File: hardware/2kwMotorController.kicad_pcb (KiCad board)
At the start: 4 copper layers, 180 x 88 mm, 259 parts, among them M1 MOUNTING_HOLE, M2 MOUNTING_HOLE, M3 MOUNTING_HOLE, M4 MOUNTING_HOLE, M5 MOUNTING_HOLE, M6 MOUNTING_HOLE, P1 CONN_01X02_CBAT, P10 CONN_01_BRK, P11 CONN_01_M+, P12 CONN_01_M-, P13 CONN_01X02_MTMP, P14 CONN_01X02_BTMP, P2 CONN_01X02_FAN, P3 CONN_01X09, P4 CONN_02X05_JTAG, P5 CONN_01X03_UART, P6 CONN_01X03_CAN, P7 CONN_01X05_ENCODER, P8 CONN_01_V+, P9 CONN_01_V-, Q1 DMG4712SSS, Q10 PSMN021-100, Q2 DMG4712SSS, Q3 IRFP4468, Q4 PSMN021-100, Q5 IRFP4468, Q6 IRFP4468, Q7 IRFP4468, Q8 IRFP4468, Q9 IRFP4468, SW2 SW_PUSH, U1 LM358A, U10 MCP1501T-30E, U11 PDM1-S, U12 MIC5225-5.0, U13 TM4C1294KCPDT, U14 74LVCH2T45, U15 SN65HVD231D, U16 Si8045AA, U17 MIC4127, U18 MIC4127, U19 UCC27211, U2 LAH-100P, U20 Si8045AA, U21 74LVC1G17, U3 LOC110, U4 MCP6001, U5 ADA4805-1, U6 UCC27211, U7 MIC5225-5.0, U8 LT3471, U9 R-78E3.3-0.5, Y1 NX5032GA

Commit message: All DRC/ERC passed
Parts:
- removed the REF**1111 at (193.2, 109.0)
- removed the REF**1112 at (193.2, 109.5)
- removed the REF**1113 at (193.2, 110.0)
- removed the REF**121 at (153.0, 96.8)
- removed REF**122, REF**132, REF**142: VIA-0.6mm, 2kwMotorController:VIA-0.6mm
- removed the REF**131 at (153.5, 96.8)
- removed the REF**141 at (154.0, 96.8)
- added REF**: VIA-0.6mm, 2kwMotorController:VIA-0.6mm, F.Cu at (136.5, 48.5)
- added REF**: VIA-0.6mm, 2kwMotorController:VIA-0.6mm, F.Cu at (136.0, 48.5)
- added REF**: VIA-0.6mm, 2kwMotorController:VIA-0.6mm, F.Cu at (136.5, 47.0)
- added REF**: VIA-0.6mm, 2kwMotorController:VIA-0.6mm, F.Cu at (80.2, 30.0)
- added REF**: VIA-0.6mm, 2kwMotorController:VIA-0.6mm, F.Cu at (136.0, 47.0)
- added REF**11: VIA-0.6mm, 2kwMotorController:VIA-0.6mm, F.Cu at (189.6, 100.6)
- added REF**11: VIA-0.6mm, 2kwMotorController:VIA-0.6mm, F.Cu at (54.6, 40.8)
- added REF**11: VIA-0.6mm, 2kwMotorController:VIA-0.6mm, F.Cu at (185.6, 49.7)
- added REF**11: VIA-0.6mm, 2kwMotorController:VIA-0.6mm, F.Cu at (185.1, 44.7)
- added REF**11: VIA-0.6mm, 2kwMotorController:VIA-0.6mm, F.Cu at (107.7, 74.4)
- added REF**11: VIA-0.6mm, 2kwMotorController:VIA-0.6mm, F.Cu at (106.8, 87.9)
- added REF**11: VIA-0.6mm, 2kwMotorController:VIA-0.6mm, F.Cu at (113.4, 48.0)
- added REF**11: VIA-0.6mm, 2kwMotorController:VIA-0.6mm, F.Cu at (120.4, 49.4)
- added REF**111: VIA-0.6mm, 2kwMotorController:VIA-0.6mm, F.Cu at (160.9, 100.4)
- added REF**1111: VIA-0.6mm, 2kwMotorController:VIA-0.6mm, F.Cu at (56.4, 97.2)
- added REF**1111: VIA-0.6mm, 2kwMotorController:VIA-0.6mm, F.Cu at (70.2, 49.4)
- added REF**1111: VIA-0.6mm, 2kwMotorController:VIA-0.6mm, F.Cu at (63.6, 48.0)
- added REF**11111: VIA-0.6mm, 2kwMotorController:VIA-0.6mm, F.Cu at (169.8, 106.0)
- added REF**11111: VIA-0.6mm, 2kwMotorController:VIA-0.6mm, F.Cu at (169.2, 106.0)
- added REF**1112: VIA-0.6mm, 2kwMotorController:VIA-0.6mm, F.Cu at (63.6, 48.5)
- added REF**1112: VIA-0.6mm, 2kwMotorController:VIA-0.6mm, F.Cu at (70.2, 49.9)
- added REF**1112: VIA-0.6mm, 2kwMotorController:VIA-0.6mm, F.Cu at (151.4, 97.4)
- added REF**1113: VIA-0.6mm, 2kwMotorController:VIA-0.6mm, F.Cu at (63.6, 49.0)
- added REF**1113: VIA-0.6mm, 2kwMotorController:VIA-0.6mm, F.Cu at (70.2, 50.4)
- added REF**1114: VIA-0.6mm, 2kwMotorController:VIA-0.6mm, F.Cu at (63.6, 49.5)
- added REF**1114: VIA-0.6mm, 2kwMotorController:VIA-0.6mm, F.Cu at (70.2, 50.9)
- added REF**1115: VIA-0.6mm, 2kwMotorController:VIA-0.6mm, F.Cu at (63.6, 50.0)
- added REF**1115: VIA-0.6mm, 2kwMotorController:VIA-0.6mm, F.Cu at (70.2, 51.4)
- added REF**1116: VIA-0.6mm, 2kwMotorController:VIA-0.6mm, F.Cu at (63.6, 50.5)
- added REF**1116: VIA-0.6mm, 2kwMotorController:VIA-0.6mm, F.Cu at (70.2, 51.9)
- added REF**1117: VIA-0.6mm, 2kwMotorController:VIA-0.6mm, F.Cu at (63.6, 51.0)
- added REF**1118: VIA-0.6mm, 2kwMotorController:VIA-0.6mm, F.Cu at (63.6, 51.5)
- added REF**1121: VIA-0.6mm, 2kwMotorController:VIA-0.6mm, F.Cu at (152.0, 96.8)
- added REF**1121: VIA-0.6mm, 2kwMotorController:VIA-0.6mm, F.Cu at (57.0, 97.2)
- added REF**1122: VIA-0.6mm, 2kwMotorController:VIA-0.6mm, F.Cu at (152.0, 97.4)
- added REF**113: VIA-0.6mm, 2kwMotorController:VIA-0.6mm, F.Cu at (160.9, 101.6)
- added REF**1131: VIA-0.6mm, 2kwMotorController:VIA-0.6mm, F.Cu at (152.6, 96.8)
- added REF**1131: VIA-0.6mm, 2kwMotorController:VIA-0.6mm, F.Cu at (57.6, 97.2)
- added REF**1132: VIA-0.6mm, 2kwMotorController:VIA-0.6mm, F.Cu at (152.6, 97.4)
- added REF**114: VIA-0.6mm, 2kwMotorController:VIA-0.6mm, F.Cu at (160.9, 102.2)
- added REF**1141: VIA-0.6mm, 2kwMotorController:VIA-0.6mm, F.Cu at (153.2, 96.8)
- added REF**1141: VIA-0.6mm, 2kwMotorController:VIA-0.6mm, F.Cu at (58.2, 97.2)
- added REF**1142: VIA-0.6mm, 2kwMotorController:VIA-0.6mm, F.Cu at (153.2, 97.4)
- added REF**1151: VIA-0.6mm, 2kwMotorController:VIA-0.6mm, F.Cu at (153.8, 96.8)
- added REF**1151: VIA-0.6mm, 2kwMotorController:VIA-0.6mm, F.Cu at (58.8, 97.2)
- added REF**1152: VIA-0.6mm, 2kwMotorController:VIA-0.6mm, F.Cu at (153.8, 97.4)
- added REF**1161: VIA-0.6mm, 2kwMotorController:VIA-0.6mm, F.Cu at (154.4, 96.8)
- added REF**1161: VIA-0.6mm, 2kwMotorController:VIA-0.6mm, F.Cu at (59.4, 97.2)
- added REF**1162: VIA-0.6mm, 2kwMotorController:VIA-0.6mm, F.Cu at (154.4, 97.4)
- added REF**12: VIA-0.6mm, 2kwMotorController:VIA-0.6mm, F.Cu at (120.4, 49.9)
- added REF**12: VIA-0.6mm, 2kwMotorController:VIA-0.6mm, F.Cu at (113.4, 48.5)
- added REF**12: VIA-0.6mm, 2kwMotorController:VIA-0.6mm, F.Cu at (107.7, 75.0)
- added REF**12: VIA-0.6mm, 2kwMotorController:VIA-0.6mm, F.Cu at (185.1, 45.3)
- added REF**12: VIA-0.6mm, 2kwMotorController:VIA-0.6mm, F.Cu at (189.6, 101.2)
- added REF**13: VIA-0.6mm, 2kwMotorController:VIA-0.6mm, F.Cu at (120.4, 50.4)
- added REF**13: VIA-0.6mm, 2kwMotorController:VIA-0.6mm, F.Cu at (113.4, 49.0)
- added REF**13: VIA-0.6mm, 2kwMotorController:VIA-0.6mm, F.Cu at (107.7, 75.6)
- added REF**13: VIA-0.6mm, 2kwMotorController:VIA-0.6mm, F.Cu at (185.1, 45.9)
- added REF**14: VIA-0.6mm, 2kwMotorController:VIA-0.6mm, F.Cu at (120.4, 50.9)
- added REF**14: VIA-0.6mm, 2kwMotorController:VIA-0.6mm, F.Cu at (113.4, 49.5)
- added REF**14: VIA-0.6mm, 2kwMotorController:VIA-0.6mm, F.Cu at (107.7, 76.2)
- added REF**15: VIA-0.6mm, 2kwMotorController:VIA-0.6mm, F.Cu at (120.4, 51.4)
- added REF**15: VIA-0.6mm, 2kwMotorController:VIA-0.6mm, F.Cu at (113.4, 50.0)
- added REF**16: VIA-0.6mm, 2kwMotorController:VIA-0.6mm, F.Cu at (120.4, 51.9)
- added REF**16: VIA-0.6mm, 2kwMotorController:VIA-0.6mm, F.Cu at (113.4, 50.5)
- added REF**17: VIA-0.6mm, 2kwMotorController:VIA-0.6mm, F.Cu at (113.4, 51.0)
- added REF**18: VIA-0.6mm, 2kwMotorController:VIA-0.6mm, F.Cu at (113.4, 51.5)
- added REF**21: VIA-0.6mm, 2kwMotorController:VIA-0.6mm, F.Cu at (107.4, 87.9)
- added REF**21: VIA-0.6mm, 2kwMotorController:VIA-0.6mm, F.Cu at (186.2, 49.7)
- added REF**21: VIA-0.6mm, 2kwMotorController:VIA-0.6mm, F.Cu at (55.2, 40.8)
- added REF**21: VIA-0.6mm, 2kwMotorController:VIA-0.6mm, F.Cu at (190.2, 100.6)
- added REF**22: VIA-0.6mm, 2kwMotorController:VIA-0.6mm, F.Cu at (190.2, 101.2)
- added REF**31: VIA-0.6mm, 2kwMotorController:VIA-0.6mm, F.Cu at (108.0, 87.9)
- added REF**31: VIA-0.6mm, 2kwMotorController:VIA-0.6mm, F.Cu at (186.8, 49.7)
- added REF**31: VIA-0.6mm, 2kwMotorController:VIA-0.6mm, F.Cu at (55.8, 40.8)
- added REF**31: VIA-0.6mm, 2kwMotorController:VIA-0.6mm, F.Cu at (190.8, 100.6)
- added REF**32: VIA-0.6mm, 2kwMotorController:VIA-0.6mm, F.Cu at (190.8, 101.2)
- added REF**41: VIA-0.6mm, 2kwMotorController:VIA-0.6mm, F.Cu at (108.6, 87.9)
- added REF**41: VIA-0.6mm, 2kwMotorController:VIA-0.6mm, F.Cu at (187.4, 49.7)
- added REF**41: VIA-0.6mm, 2kwMotorController:VIA-0.6mm, F.Cu at (56.4, 40.8)
- added REF**41: VIA-0.6mm, 2kwMotorController:VIA-0.6mm, F.Cu at (191.4, 100.6)
- added REF**42: VIA-0.6mm, 2kwMotorController:VIA-0.6mm, F.Cu at (191.4, 101.2)
- added REF**51: VIA-0.6mm, 2kwMotorController:VIA-0.6mm, F.Cu at (57.0, 40.8)
- added REF**61: VIA-0.6mm, 2kwMotorController:VIA-0.6mm, F.Cu at (57.6, 40.8)
- added REF**6111: VIA-0.6mm, 2kwMotorController:VIA-0.6mm, F.Cu at (169.8, 98.2)
- added REF**6112: VIA-0.6mm, 2kwMotorController:VIA-0.6mm, F.Cu at (169.8, 98.8)
- added REF**6113: VIA-0.6mm, 2kwMotorController:VIA-0.6mm, F.Cu at (169.8, 99.4)
- added REF**6121: VIA-0.6mm, 2kwMotorController:VIA-0.6mm, F.Cu at (170.4, 98.2)
- added REF**6122: VIA-0.6mm, 2kwMotorController:VIA-0.6mm, F.Cu at (170.4, 98.8)
- added REF**6123: VIA-0.6mm, 2kwMotorController:VIA-0.6mm, F.Cu at (170.4, 99.4)
- added REF**6131: VIA-0.6mm, 2kwMotorController:VIA-0.6mm, F.Cu at (171.1, 98.2)
- added REF**6132: VIA-0.6mm, 2kwMotorController:VIA-0.6mm, F.Cu at (171.1, 98.8)
- added REF**6133: VIA-0.6mm, 2kwMotorController:VIA-0.6mm, F.Cu at (171.1, 99.4)
- added REF**6141: VIA-0.6mm, 2kwMotorController:VIA-0.6mm, F.Cu at (171.7, 98.2)
- added REF**6142: VIA-0.6mm, 2kwMotorController:VIA-0.6mm, F.Cu at (171.7, 98.8)
- added REF**6143: VIA-0.6mm, 2kwMotorController:VIA-0.6mm, F.Cu at (171.7, 99.4)
- added REF**6151: VIA-0.6mm, 2kwMotorController:VIA-0.6mm, F.Cu at (172.2, 98.2)
- added REF**6152: VIA-0.6mm, 2kwMotorController:VIA-0.6mm, F.Cu at (172.2, 98.8)
- added REF**6153: VIA-0.6mm, 2kwMotorController:VIA-0.6mm, F.Cu at (172.2, 99.4)
- added REF**6161: VIA-0.6mm, 2kwMotorController:VIA-0.6mm, F.Cu at (172.8, 98.2)
- added REF**6162: VIA-0.6mm, 2kwMotorController:VIA-0.6mm, F.Cu at (172.8, 98.8)
- added REF**6163: VIA-0.6mm, 2kwMotorController:VIA-0.6mm, F.Cu at (172.8, 99.4)
- added REF**6171: VIA-0.6mm, 2kwMotorController:VIA-0.6mm, F.Cu at (173.4, 98.2)
- added REF**6172: VIA-0.6mm, 2kwMotorController:VIA-0.6mm, F.Cu at (173.4, 98.8)
- added REF**6173: VIA-0.6mm, 2kwMotorController:VIA-0.6mm, F.Cu at (173.4, 99.4)
- added TP1: TEST_POINT, 2kwMotorController:TEST_PAD_1.27mm, F.Cu at (151.0, 35.8)
- added TP10: TEST_POINT, 2kwMotorController:TEST_PAD_1.27mm, F.Cu at (194.8, 100.0)
- added TP11: TEST_POINT, 2kwMotorController:TEST_PAD_1.27mm, F.Cu at (198.8, 63.0)
- added TP12: TEST_POINT, 2kwMotorController:TEST_PAD_1.27mm, F.Cu at (188.8, 42.8)
- added TP13: TEST_POINT, 2kwMotorController:TEST_PAD_1.27mm, F.Cu at (149.0, 98.6)
- added TP14: TEST_POINT, 2kwMotorController:TEST_PAD_1.27mm, F.Cu at (174.8, 101.4)
- added TP15: TEST_POINT, 2kwMotorController:TEST_PAD_1.27mm, F.Cu at (181.6, 99.8)
- added TP16: TEST_POINT, 2kwMotorController:TEST_PAD_1.27mm, F.Cu at (130.2, 52.6)
- added TP17: TEST_POINT, 2kwMotorController:TEST_PAD_1.27mm, F.Cu at (182.0, 114.0)
- added TP18: TEST_POINT, 2kwMotorController:TEST_PAD_1.27mm, F.Cu at (139.4, 48.0)
- added TP19: TEST_POINT, 2kwMotorController:TEST_PAD_1.27mm, F.Cu at (187.8, 83.0)
- added TP2: TEST_POINT, 2kwMotorController:TEST_PAD_1.27mm, F.Cu at (183.0, 49.4)
- added TP20: TEST_POINT, 2kwMotorController:TEST_PAD_1.27mm, F.Cu at (190.0, 83.0)
- added TP21: TEST_POINT, 2kwMotorController:TEST_PAD_1.27mm, F.Cu at (197.4, 81.0)
- added TP22: TEST_POINT, 2kwMotorController:TEST_PAD_1.27mm, F.Cu at (195.4, 88.8)
- added TP23: TEST_POINT, 2kwMotorController:TEST_PAD_1.27mm, F.Cu at (185.2, 58.2)
- added TP27: TEST_POINT, 2kwMotorController:TEST_PAD_1.27mm, F.Cu at (64.0, 110.0)
- added TP28: TEST_POINT, 2kwMotorController:TEST_PAD_1.27mm, F.Cu at (60.5, 110.0)
- added TP29: TEST_POINT, 2kwMotorController:TEST_PAD_1.27mm, F.Cu at (63.5, 33.0)
- added TP3: TEST_POINT, 2kwMotorController:TEST_PAD_1.27mm, F.Cu at (156.5, 52.2)
- added TP31: TEST_POINT, 2kwMotorController:TEST_PAD_1.27mm, F.Cu at (74.5, 79.8)
- added TP33: TEST_POINT, 2kwMotorController:TEST_PAD_1.27mm, F.Cu at (106.2, 62.2)
- added TP35: TEST_POINT, 2kwMotorController:TEST_PAD_1.27mm, F.Cu at (108.5, 71.8)
- added TP36: TEST_POINT, 2kwMotorController:TEST_PAD_1.27mm, F.Cu at (78.0, 70.8)
- added TP38: TEST_POINT, 2kwMotorController:TEST_PAD_1.27mm, F.Cu at (76.0, 62.5)
- added TP4: TEST_POINT, 2kwMotorController:TEST_PAD_1.27mm, F.Cu at (166.6, 41.8)
- added TP40: TEST_POINT, 2kwMotorController:TEST_PAD_1.27mm, F.Cu at (109.3, 76.2)
- added TP5: TEST_POINT, 2kwMotorController:TEST_PAD_1.27mm, F.Cu at (164.0, 49.4)
- added TP6: TEST_POINT, 2kwMotorController:TEST_PAD_1.27mm, F.Cu at (172.4, 37.6)
- added TP7: TEST_POINT, 2kwMotorController:TEST_PAD_1.27mm, F.Cu at (188.2, 39.8)
- added TP8: TEST_POINT, 2kwMotorController:TEST_PAD_1.27mm, F.Cu at (187.4, 30.2)
- added TP9: TEST_POINT, 2kwMotorController:TEST_PAD_1.27mm, F.Cu at (171.1, 96.2)
- C35, C36, C39, C41, C45: moved to B.Cu
- C40: moved to F.Cu
- Q10, Q4: footprint 2kwMotorController:SOT-669_LFPAK_ThermalVias-1 -> 2kwMotorController:SOT-669_LFPAK
- moved C59 31.3 mm to (64.0, 48.5), turned to 180 degrees
- moved C62 22.7 mm to (68.5, 49.8), turned to 0 degrees
- moved C56 16.1 mm to (64.0, 51.0)
- moved C61 15.6 mm to (68.5, 51.5)
- moved C68 13.8 mm to (113.8, 48.5), turned to 180 degrees
- moved REF**112 9.24 mm to (160.9, 101.0)
- moved C65 7.50 mm to (118.5, 49.8)
- moved C32 7.25 mm to (172.2, 61.3), turned to 90 degrees
- moved C36 7.24 mm to (176.5, 61.7), turned to 90 degrees
- moved C40 7.09 mm to (182.5, 59.6), turned to 0 degrees
- moved C45 5.99 mm to (168.4, 56.3), turned to 0 degrees
- moved C35 5.82 mm to (165.8, 59.8), turned to 0 degrees
- moved C41 5.65 mm to (167.5, 67.8), turned to 180 degrees
- moved C66 5.46 mm to (113.8, 51.0), turned to 180 degrees
- moved C39 5.46 mm to (176.4, 56.9), turned to 270 degrees
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- renumbered REF**111 to REF**1111
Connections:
- net Net-(C2-Pad1) renamed /sensors/ISENSE_OUT
- net Net-(D8-Pad2) renamed /power/FAN_DRAIN
- net Net-(Q10-Pad1) renamed /h-bridge/VBUS_ST_GATE_1
- net Net-(Q2-Pad4) renamed /power/FAN_GATE
- net Net-(Q3-Pad1) renamed /h-bridge/VBUS_EN_GATE
- net Net-(Q4-Pad1) renamed /h-bridge/VBUS_ST_GATE_2
- net Net-(Q5-Pad1) renamed /h-bridge/VBUS_BRK_GATE
- net Net-(R1-Pad2) renamed /sensors/VBUS_DIV
- net Net-(R5-Pad1) renamed /sensors/IS_SUM
- C75 pad 2: GNDA -> GND
- REF**112 pad 1: -12V -> GND
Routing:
- net /h-bridge/VBUS: track 135.7 -> 185.8 mm, vias 1 -> 2
- net +12V_ISO: track 241.4 -> 288.2 mm, vias 9 -> 2
- net GND: track 147.6 -> 185.7 mm, vias 72 -> 85
- net GNDPWR: track 141.8 -> 168.8 mm, vias 21 -> 32
- net /h-bridge/VBUS_ST_GD: track 132.9 -> 158.0 mm
- net /mcu/JTAG_RST_N: track 9.35 -> 34.5 mm, vias 0 -> 4
- net /h-bridge/LO_1: track 5.33 -> 29.2 mm
- net /h-bridge/LO_2: track 5.06 -> 28.5 mm
- net +12V: track 83.9 -> 106.2 mm
- net /h-bridge/VBUS_EN_GD: track 86.1 -> 107.0 mm, vias 3 -> 4
- net /h-bridge/VBUS_DIS_GD: track 124.3 -> 142.7 mm
- net +3VA: track 10.9 -> 28.1 mm, vias 1 -> 2
- net Net-(C3-Pad1): track 17.0 -> 33.4 mm, vias 0 -> 2
- net /power/FAN_DRAIN: track 12.8 -> 26.4 mm, vias 0 -> 5
- net Net-(C3-Pad2): track 7.30 -> 15.8 mm
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- added copper zone on B.Cu, net +12V_ISO
- added copper zone on In2.Cu, net +12V_ISO
- added copper zone on F.Cu, net +3V3
- added copper zone on F.Cu, net /h-bridge/VBUS
- added copper zone on In2.Cu, net /power/FAN_DRAIN
- removed copper zone on In2.Cu, net /h-bridge/LO_1
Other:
- board text added: "+12V_ISO"
- board text added: "- +"

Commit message: tweaks, testpoints, decluttering
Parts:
- removed TP27, TP28, TP29: TEST_POINT, 2kwMotorController:TEST_PAD_1.27mm
- added GND: GND_POINT, 2kwMotorController:TEST_PAD_1.27mm, F.Cu at (157.0, 30.2)
- added GND: GND_POINT, 2kwMotorController:TEST_PAD_1.27mm, F.Cu at (179.6, 39.0)
- added GND: GND_POINT, 2kwMotorController:TEST_PAD_1.27mm, F.Cu at (196.6, 59.4)
- added GND: GND_POINT, 2kwMotorController:TEST_PAD_1.27mm, F.Cu at (170.6, 92.2)
- added GND: GND_POINT, 2kwMotorController:TEST_PAD_1.27mm, F.Cu at (184.4, 75.8)
- added GND: GND_POINT, 2kwMotorController:TEST_PAD_1.27mm, F.Cu at (158.0, 113.8)
- added GND: GND_POINT, 2kwMotorController:TEST_PAD_1.27mm, F.Cu at (194.2, 93.2)
- added GNDPWR: GND_POINT, 2kwMotorController:TEST_PAD_1.27mm, F.Cu at (97.4, 62.0)
- added GNDPWR: GND_POINT, 2kwMotorController:TEST_PAD_1.27mm, F.Cu at (66.8, 93.6)
- added GNDPWR: GND_POINT, 2kwMotorController:TEST_PAD_1.27mm, F.Cu at (66.6, 39.4)
- added GNDPWR: GND_POINT, 2kwMotorController:TEST_PAD_1.27mm, F.Cu at (72.8, 82.4)
- added GNDPWR: GND_POINT, 2kwMotorController:TEST_PAD_1.27mm, F.Cu at (129.4, 63.0)
- U9: moved to F.Cu
- moved C29 9.51 mm to (180.5, 94.0)
- moved C31 9.51 mm to (184.0, 94.0)
- moved U14 9.45 mm to (182.2, 96.8)
- moved R62 9.25 mm to (187.2, 94.5)
- moved R63 7.75 mm to (189.2, 95.2), turned to 270 degrees
- moved U9 5.10 mm to (203.4, 63.0), turned to 0 degrees
- moved R26 3.75 mm to (193.5, 65.2), turned to 270 degrees
- moved P4 3.61 mm to (191.0, 65.8)
- moved TP10 2.80 mm to (194.8, 97.2)
- moved TP15 1.71 mm to (183.2, 100.2)
- moved C11 1.50 mm to (197.2, 100.9)
- moved C7 1.50 mm to (190.2, 101.8)
- moved D10 1.50 mm to (188.4, 75.1)
- moved D11 1.50 mm to (188.4, 72.1)
- moved D12 1.50 mm to (188.4, 69.1)
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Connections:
- net Net-(JP1-Pad1) renamed /mcu/FRST
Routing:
- net /h-bridge/VBUS_ST_GD: track 158.0 -> 132.3 mm
- net /h-bridge/VBUS_DIS_GD: track 142.7 -> 121.6 mm
- net /h-bridge/VBUS_EN_GD: track 107.0 -> 86.6 mm, vias 4 -> 3
- net /mcu/ENCODER_CHA: track 7.85 -> 18.3 mm
- net /mcu/QEI_PHB: track 42.5 -> 33.0 mm
- net /mcu/ENCODER_CHB: track 8.05 -> 17.6 mm
- net /mcu/QEI_PHA: track 42.9 -> 33.5 mm
- net +BATT: track 152.1 -> 146.0 mm
- net /mcu/JTAG_RST_N: track 34.5 -> 39.7 mm
- net /mcu/LED_3: track 16.2 -> 12.2 mm
- net /mcu/PWM_FAN: track 43.3 -> 39.4 mm, vias 4 -> 2
- net /mcu/JTAG_TCK: track 8.00 -> 11.8 mm, vias 0 -> 1
- net /mcu/JTAG_TMS: track 7.92 -> 11.5 mm, vias 0 -> 1
- net /mcu/LED_1: track 18.3 -> 14.8 mm
- net /mcu/JTAG_TDI: track 11.4 -> 13.8 mm, vias 1 -> 0
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- added copper zone on F.Cu, net Net-(C51-Pad2)
- added copper zone on F.Cu, net Net-(C52-Pad1)

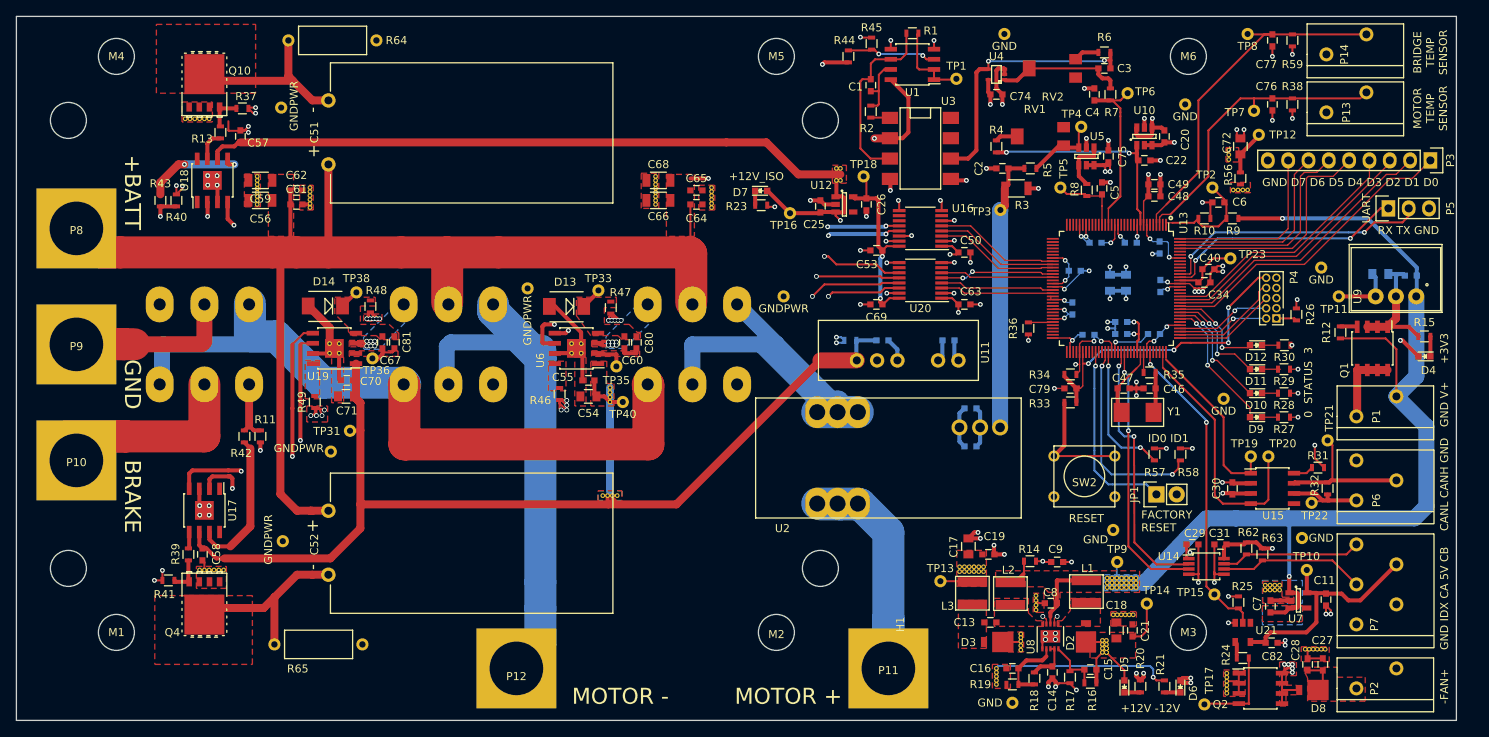
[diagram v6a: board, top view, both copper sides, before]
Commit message: Rev 0 board finished and submitted for manufacture
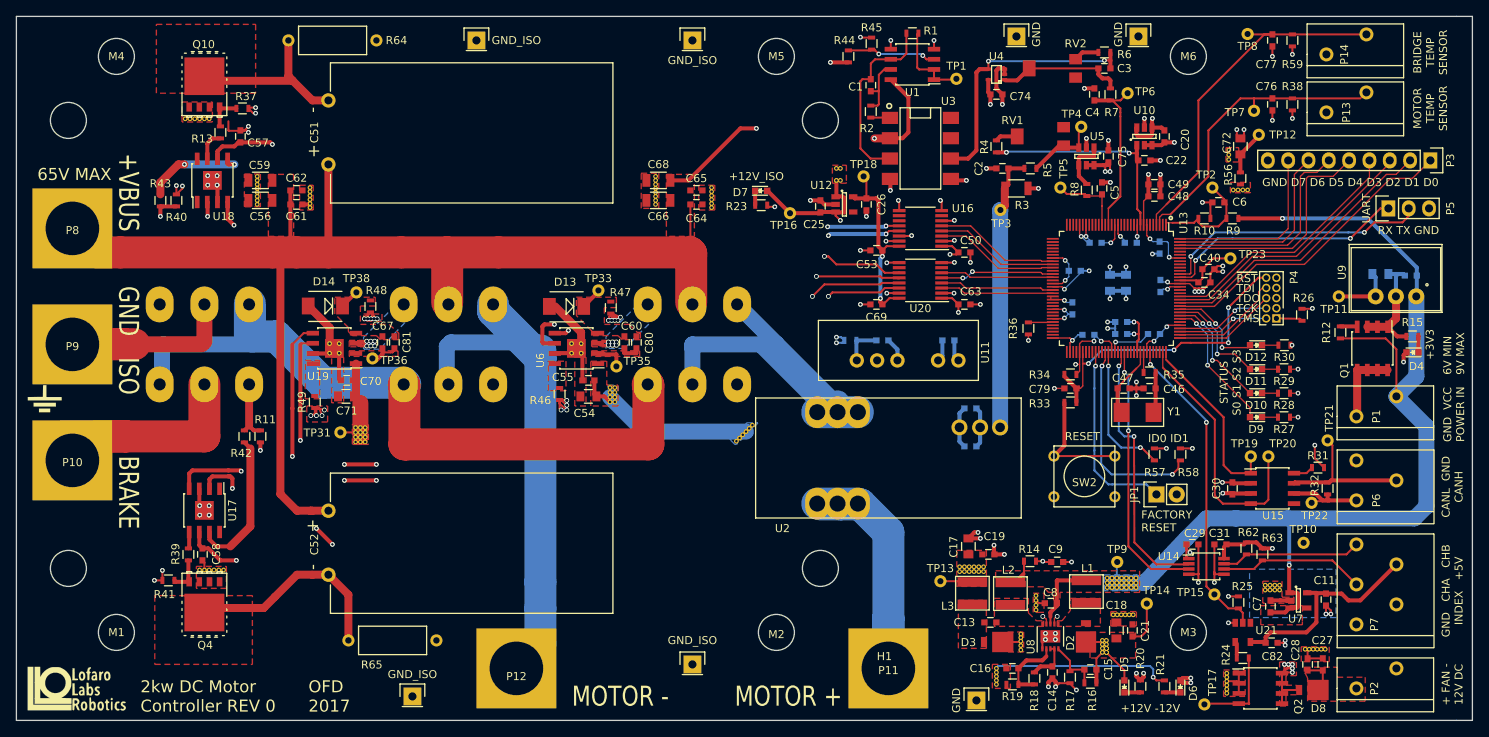
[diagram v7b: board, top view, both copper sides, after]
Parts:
- removed the GND at (157.0, 30.2)
- removed the GND at (179.6, 39.0)
- removed the GND at (196.6, 59.4)
- removed the GND at (170.6, 92.2)
- removed the GND at (184.4, 75.8)
- removed the GND at (158.0, 113.8)
- removed the GND at (194.2, 93.2)
- removed GNDPWR (x5): GND_POINT, 2kwMotorController:TEST_PAD_1.27mm
- removed TP40: TEST_POINT, 2kwMotorController:TEST_PAD_1.27mm
- added G***: LOGO, 2kwMotorController:lofaro-labs-logo, F.Cu at (41.0, 112.0)
- added G***: LOGO, 2kwMotorController:gnd-symbol, F.Cu at (37.0, 75.8)
- added GND: GND_POINT, Pin_Headers:Pin_Header_Straight_1x01, F.Cu at (153.5, 113.5)
- added GND: GND_POINT, Pin_Headers:Pin_Header_Straight_1x01, F.Cu at (158.5, 30.5)
- added GND: GND_POINT, Pin_Headers:Pin_Header_Straight_1x01, F.Cu at (173.8, 30.5)
- added GND_ISO: GND_POINT, Pin_Headers:Pin_Header_Straight_1x01, F.Cu at (83.0, 113.0)
- added GND_ISO: GND_POINT, Pin_Headers:Pin_Header_Straight_1x01, F.Cu at (118.0, 109.0)
- added GND_ISO: GND_POINT, Pin_Headers:Pin_Header_Straight_1x01, F.Cu at (91.0, 31.0)
- added GND_ISO: GND_POINT, Pin_Headers:Pin_Header_Straight_1x01, F.Cu at (118.0, 31.0)
- added REF**11: VIA-0.6mm, 2kwMotorController:VIA-0.6mm, F.Cu at (123.5, 81.1)
- added REF**11: VIA-0.6mm, 2kwMotorController:VIA-0.6mm, F.Cu at (108.3, 76.2)
- added REF**11: VIA-0.6mm, 2kwMotorController:VIA-0.6mm, F.Cu at (108.3, 75.6)
- added REF**11: VIA-0.6mm, 2kwMotorController:VIA-0.6mm, F.Cu at (108.3, 75.0)
- added REF**11: VIA-0.6mm, 2kwMotorController:VIA-0.6mm, F.Cu at (108.3, 74.4)
- added REF**111: VIA-0.6mm, 2kwMotorController:VIA-0.6mm, F.Cu at (75.9, 79.4)
- added REF**112: VIA-0.6mm, 2kwMotorController:VIA-0.6mm, F.Cu at (75.9, 80.0)
- added REF**113: VIA-0.6mm, 2kwMotorController:VIA-0.6mm, F.Cu at (75.9, 80.6)
- added REF**114: VIA-0.6mm, 2kwMotorController:VIA-0.6mm, F.Cu at (75.9, 81.2)
- added REF**121: VIA-0.6mm, 2kwMotorController:VIA-0.6mm, F.Cu at (76.5, 79.4)
- added REF**122: VIA-0.6mm, 2kwMotorController:VIA-0.6mm, F.Cu at (76.5, 80.0)
- added REF**123: VIA-0.6mm, 2kwMotorController:VIA-0.6mm, F.Cu at (76.5, 80.6)
- added REF**124: VIA-0.6mm, 2kwMotorController:VIA-0.6mm, F.Cu at (76.5, 81.2)
- added REF**131: VIA-0.6mm, 2kwMotorController:VIA-0.6mm, F.Cu at (77.1, 79.4)
- added REF**132: VIA-0.6mm, 2kwMotorController:VIA-0.6mm, F.Cu at (77.1, 80.0)
- added REF**133: VIA-0.6mm, 2kwMotorController:VIA-0.6mm, F.Cu at (77.1, 80.6)
- added REF**134: VIA-0.6mm, 2kwMotorController:VIA-0.6mm, F.Cu at (77.1, 81.2)
- added REF**41: VIA-0.6mm, 2kwMotorController:VIA-0.6mm, F.Cu at (125.5, 79.1)
- Q10, Q4: footprint 2kwMotorController:SOT-669_LFPAK -> 2kwMotorController:SOT-669_LFPAK_PASTE
- moved REF**11 18.6 mm to (123.9, 80.7), turned to 90 degrees
- moved REF**21 18.5 mm to (124.3, 80.3), turned to 90 degrees
- moved REF**31 18.5 mm to (124.7, 79.9), turned to 90 degrees
- moved REF**41 18.5 mm to (125.1, 79.5), turned to 90 degrees
- moved R65 9.26 mm to (75.0, 106.0)
- moved TP10 3.42 mm to (194.4, 93.8)
- moved D4 1.58 mm to (208.0, 70.0)
- moved R15 1.50 mm to (208.0, 68.0)
- moved TP31 1.22 mm to (74.0, 80.0)
- moved R26 0.70 mm to (194.2, 65.3)
- moved P10 0.50 mm to (40.5, 83.5)
- moved P8 0.50 mm to (40.5, 54.5)
- moved P9 0.50 mm to (40.5, 69.0)
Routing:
- net +5V: track 43.7 -> 52.0 mm
- net Net-(C52-Pad1): track 23.2 -> 26.5 mm
- net /h-bridge/VBUS: track 185.8 -> 188.9 mm
- net /h-bridge/PWM3_GD: track 109.5 -> 107.1 mm, vias 2 -> 4
- net /h-bridge/VBUS_DIS_GD: track 121.6 -> 123.8 mm, vias 2 -> 4
- net +3V3: track 74.9 -> 73.4 mm
- net +12V_ISO: track 287.5 -> 289.0 mm, vias 2 -> 4
- net /h-bridge/BRAKE: track 31.4 -> 32.4 mm
- net GNDMBAT: track 27.1 -> 28.1 mm
- net Net-(P4-Pad1): track 2.96 -> 3.66 mm
- net GND: track 185.7 -> 185.1 mm
- net Net-(D4-Pad1): track 2.50 -> 2.00 mm
- net /h-bridge/PWM4_GD: track 102.7 -> 102.3 mm, vias 2 -> 4
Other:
- board size 180 x 88 mm -> 182 x 88 mm
- rule via_min_drill: 0.3 -> 0.0762
- rule via_min_size: 0.6 -> 0.1524
- board text added: "+ FAN - 12V DC"
- board text added: "+VBUS"
- board text added: "2kw DC Motor Controller REV 0"
- board text added: "65V MAX"
- board text added: "6V MIN 9V MAX"
- board text added: "CANL GND CANH"
- board text added: "GND CHA CHB INDEX +5V"
- board text added: "GND ISO"
- board text added: "GND VCC POWER IN"
- board text added: "OFD 2017"
- board text added: "STATUS S0 S1 S2 S3"
- board text added: "TCK"
- board text added: "TDI"
- board text added: "TDO"
- board text added: "TMS"
- board text added: "~RST"
- board text removed: "+BATT"
- board text removed: "-FAN+"
- board text removed: "0 STATUS 3"
- board text removed: "CANL CANH GND"
- board text removed: "GND"
- board text removed: "GND IDX CA 5V CB"
- board text removed: "GND V+"
